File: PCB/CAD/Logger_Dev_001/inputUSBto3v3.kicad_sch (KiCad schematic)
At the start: 32 parts, among them J4 Connector, USB-TYPE-C-16P, Q1 BC847BS, U5 AMS1117, U6 CP2102-GMR

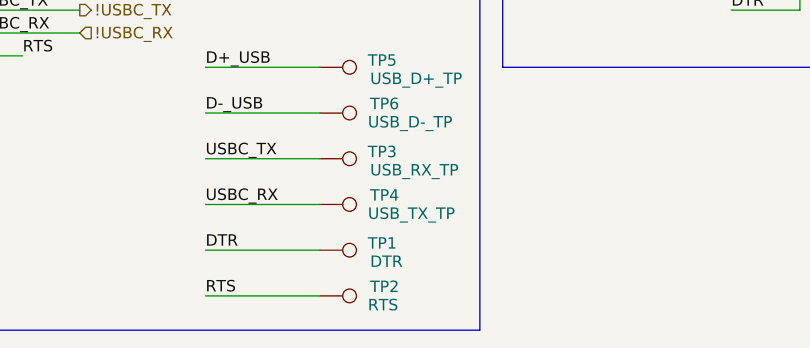
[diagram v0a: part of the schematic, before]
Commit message: Update some footprints
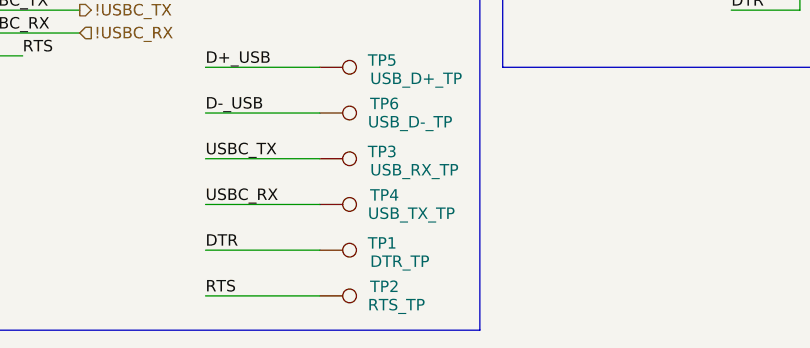
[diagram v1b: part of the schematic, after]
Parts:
- FL1: footprint DLM11SN900HY2L:FIL_DLM11SN900HY2L -> Common mode choke DLM11SN900HY2L:FIL_DLM11SN900HY2L
- TP1: value DTR -> DTR_TP
- TP2: value RTS -> RTS_TP
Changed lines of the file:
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@@
 			)
 		)
-		(property "Value" "DTR"
+		(property "Value" "DTR_TP"
 			(at 142.748 185.42 90)
 			(effects
@@
 			)
 		)
-		(property "Footprint" "DLM11SN900HY2L:FIL_DLM11SN900HY2L"
+		(property "Footprint" "Common mode choke DLM11SN900HY2L:FIL_DLM11SN900HY2L"
 			(at 119.38 49.53 0)
 			(effects
@@
 			)
 		)
-		(property "Value" "RTS"
+		(property "Value" "RTS_TP"
 			(at 142.494 190.246 90)
 			(effects

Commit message: Schematic Finished
Still need to check BOM
Starting to layout PCB
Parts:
- TP1, TP2, TP3, TP4, TP5, TP6: footprint (none) -> TestPoint:TestPoint_Pad_D2.5mm
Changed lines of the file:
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@@
 			)
 		)
-		(property "Footprint" ""
+		(property "Footprint" "TestPoint:TestPoint_Pad_D2.5mm"
 			(at 137.16 184.15 0)
 			(effects
@@
 			)
 		)
-		(property "Footprint" ""
+		(property "Footprint" "TestPoint:TestPoint_Pad_D2.5mm"
 			(at 137.16 168.91 0)
 			(effects
@@
 			)
 		)
-		(property "Footprint" ""
+		(property "Footprint" "TestPoint:TestPoint_Pad_D2.5mm"
 			(at 137.16 158.75 0)
 			(effects
@@
 			)
 		)
-		(property "Footprint" ""
+		(property "Footprint" "TestPoint:TestPoint_Pad_D2.5mm"
 			(at 137.16 179.07 0)
 			(effects
@@
 			)
 		)
-		(property "Footprint" ""
+		(property "Footprint" "TestPoint:TestPoint_Pad_D2.5mm"
 			(at 137.16 194.31 0)
 			(effects
@@
 			)
 		)
-		(property "Footprint" ""
+		(property "Footprint" "TestPoint:TestPoint_Pad_D2.5mm"
 			(at 137.16 173.99 0)
 			(effects

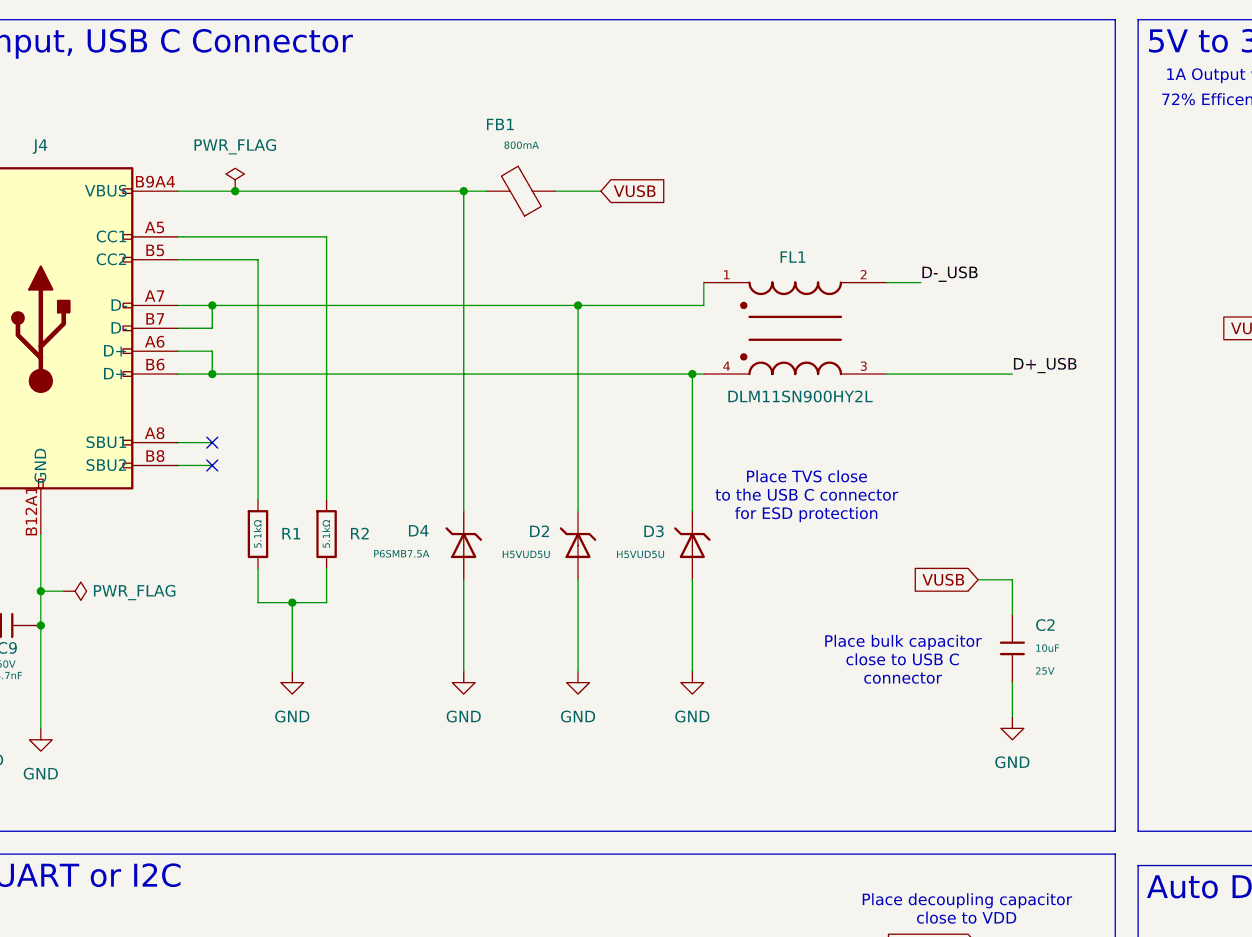
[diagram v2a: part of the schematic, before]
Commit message: PCB Layout Update
PCB Board Fixed
Most Components except Resistors placed
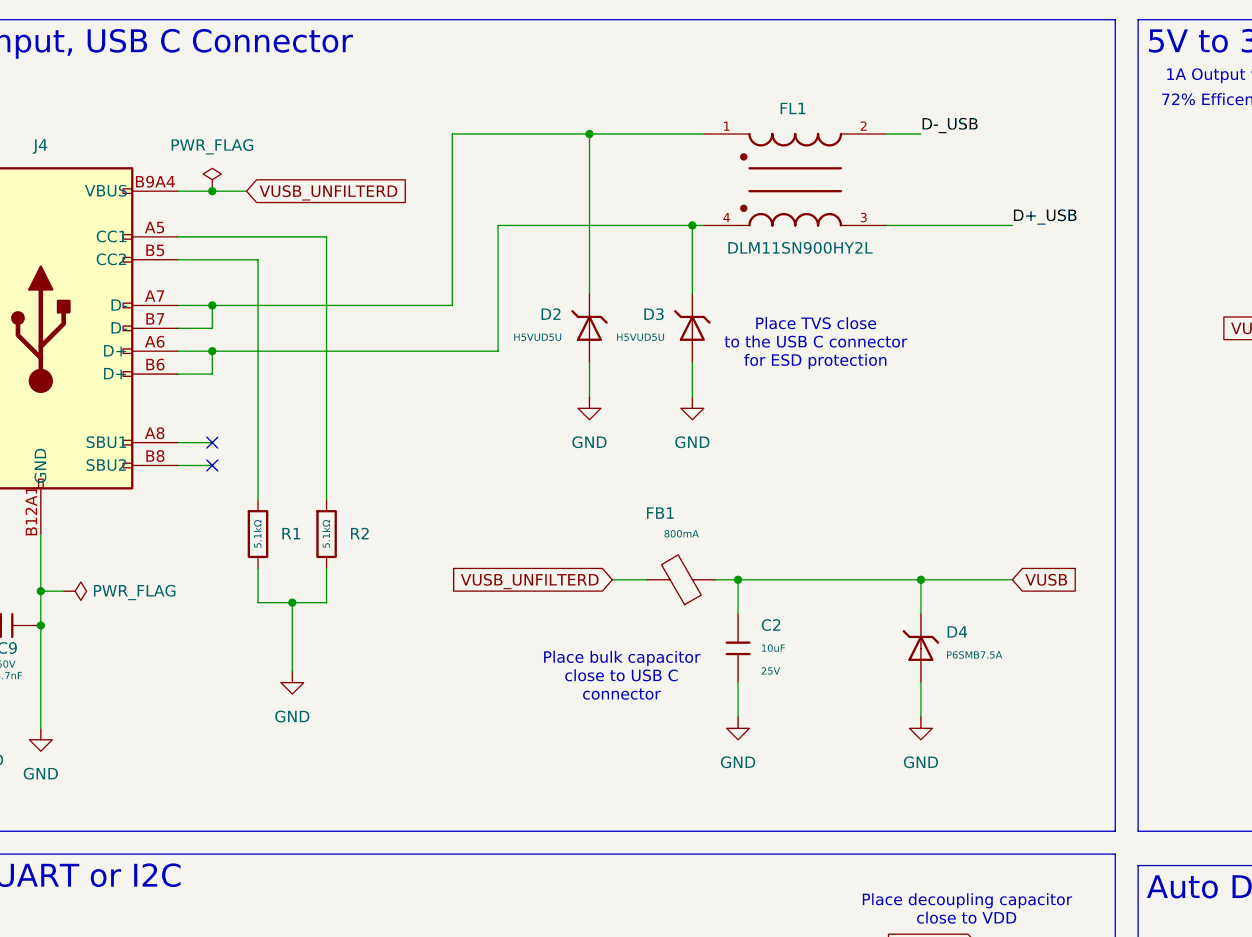
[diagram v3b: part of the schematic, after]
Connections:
- net VUSB: now also D4.1
- net VUSB_UNFILTERD: now reaches FB1.2, J4.A9B4 (VBUS), J4.B9A4 (VBUS)
- net VUSB_UNFILTERD: no longer D4.1
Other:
- moved on the sheet: C2, D2, D3, D4, FB1, FL1

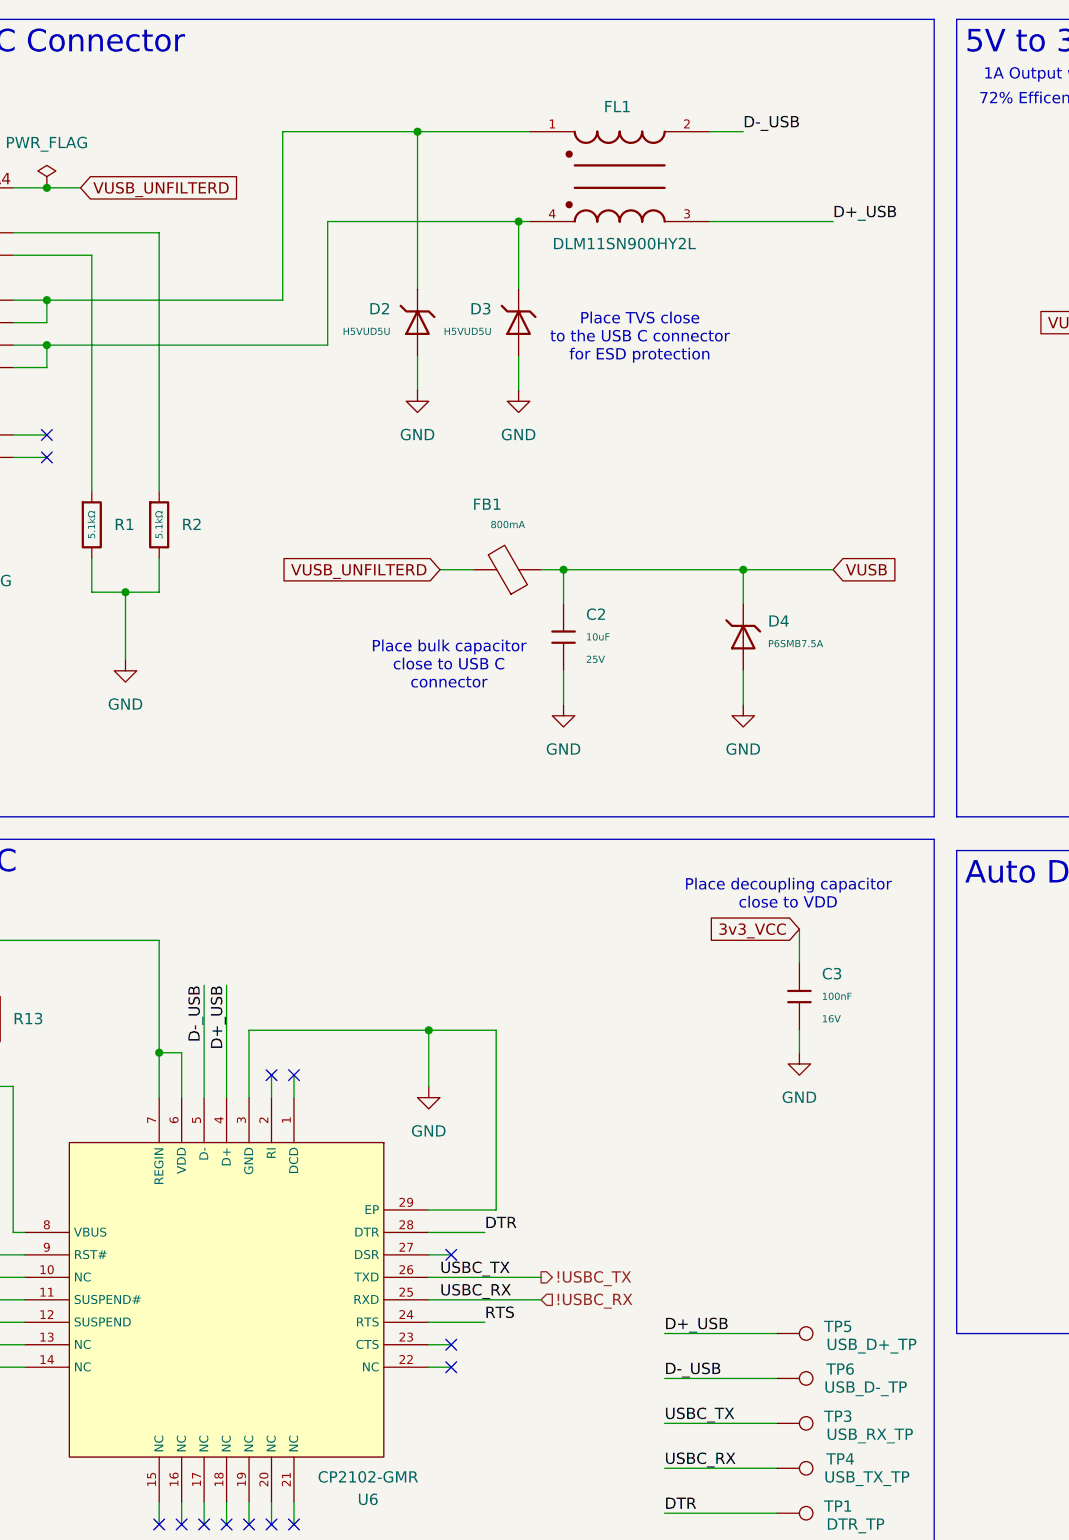
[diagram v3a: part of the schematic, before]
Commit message: PCB Board Initial Trace
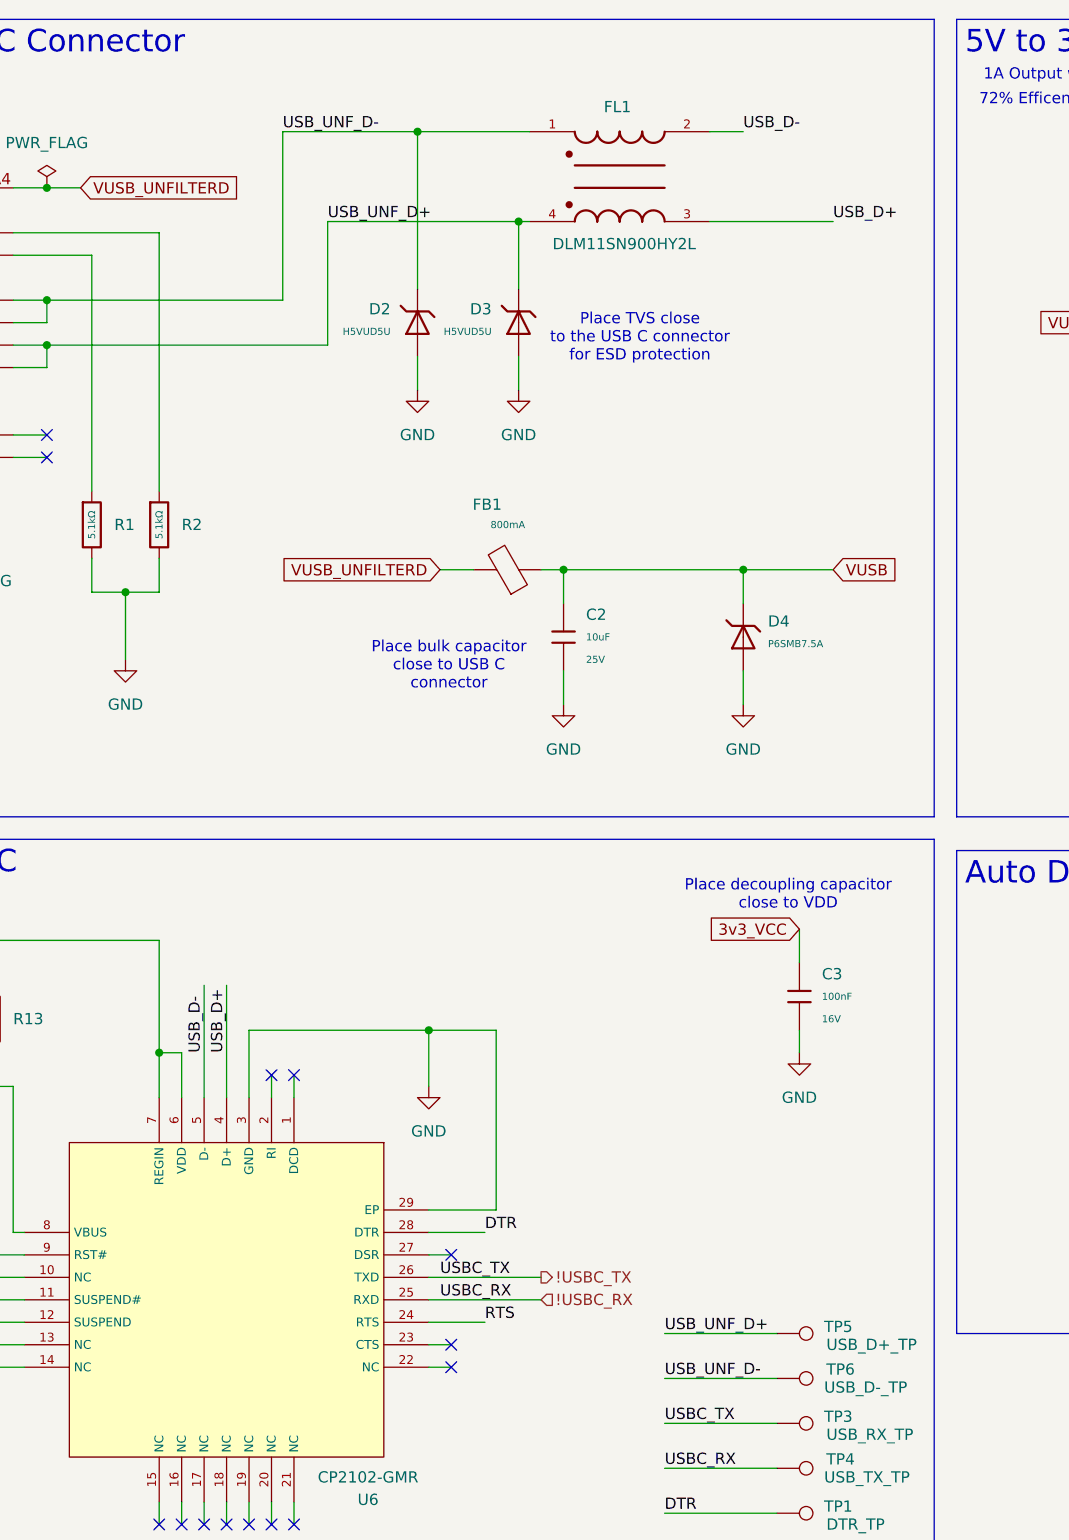
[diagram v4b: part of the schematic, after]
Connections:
- net USB_UNF_D+: now reaches D3.1, FL1.4, J4.A6 (D+), J4.B6 (D+)
- net USB_UNF_D+: now also TP5.1
- net USB_UNF_D-: now reaches D2.1, FL1.1, J4.A7 (D-), J4.B7 (D-)
- net USB_UNF_D-: now also TP6.1
- net D+_USB renamed USB_D+
- net USB_D+: no longer TP5.1
- net D-_USB renamed USB_D-
- net USB_D-: no longer TP6.1
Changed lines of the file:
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@@
 	(wire
 		(pts
-			(xy 67.31 68.58) (xy 67.31 39.37)
+			(xy 67.31 39.37) (xy 67.31 68.58)
 		)
 		(stroke
@@
 		)
 	)
-	(label "D+_USB"
+	(label "USB_UNF_D+"
+		(at 86.36 38.1 0)
+		(effects
+			(font
+				(size 1.27 1.27)
+			)
+			(justify left bottom)
+		)
+	)
+	(label "USB_UNF_D+"
 		(at 124.46 163.83 0)
 		(effects
@@
 		)
 	)
-	(label "D-_USB"
+	(label "USB_D-"
 		(at 133.35 27.94 0)
+		(effects
+			(font
+				(size 1.27 1.27)
+			)
+			(justify left bottom)
+		)
+	)
+	(label "USB_D+"
+		(at 74.93 132.08 90)
 		(effects
 			(font
@@
 		)
 	)
-	(label "D+_USB"
-		(at 74.93 124.46 270)
-		(effects
-			(font
-				(size 1.27 1.27)
-			)
-			(justify right bottom)
-		)
-	)
-	(label "D-_USB"
+	(label "USB_UNF_D-"
 		(at 124.46 168.91 0)
 		(effects
@@
 		)
 	)
+	(label "USB_UNF_D-"
+		(at 81.28 27.94 0)
+		(effects
+			(font
+				(size 1.27 1.27)
+			)
+			(justify left bottom)
+		)
+	)
 	(label "USBC_TX"
 		(at 124.46 173.99 0)
@@
 		)
 	)
-	(label "D-_USB"
-		(at 72.39 124.46 270)
-		(effects
-			(font
-				(size 1.27 1.27)
-			)
-			(justify right bottom)
-		)
-	)
-	(label "D+_USB"
+	(label "USB_D-"
+		(at 72.39 132.08 90)
+		(effects
+			(font
+				(size 1.27 1.27)
+			)
+			(justify left bottom)
+		)
+	)
+	(label "USB_D+"
 		(at 143.51 38.1 0)
 		(effects
@@
 		(polyline
 			(pts
+				(xy 57.15 59.69) (xy 57.15 72.39) (xy 74.93 72.39) (xy 74.93 62.23) (xy 69.85 59.69)
+			)
+			(stroke
+				(width 0)
+				(type dash)
+			)
+			(fill
+				(type none)
+			)
+		)
+	)
+	(rule_area
+		(polyline
+			(pts
 				(xy 231.14 38.1) (xy 231.14 59.69) (xy 278.13 59.69) (xy 278.13 44.45) (xy 271.78 38.1)
 			)
@@
 			(effects
 				(font
+					(size 1.27 1.27)
+					(italic yes)
+				)
+				(justify left)
+			)
+		)
+	)
+	(netclass_flag ""
+		(length 2.54)
+		(shape round)
+		(at 69.85 59.69 0)
+		(effects
+			(font
+				(size 1.27 1.27)
+			)
+			(justify left bottom)
+		)
+		(property "Netclass" "Signal"
+			(at 75.692 55.118 0)
+			(effects
+				(font
+					(size 1.27 1.27)
+				)
+				(justify right)
+			)
+		)
+		(property "Component Class" ""
+			(at 280.67 -48.26 0)
+			(effects
+				(font

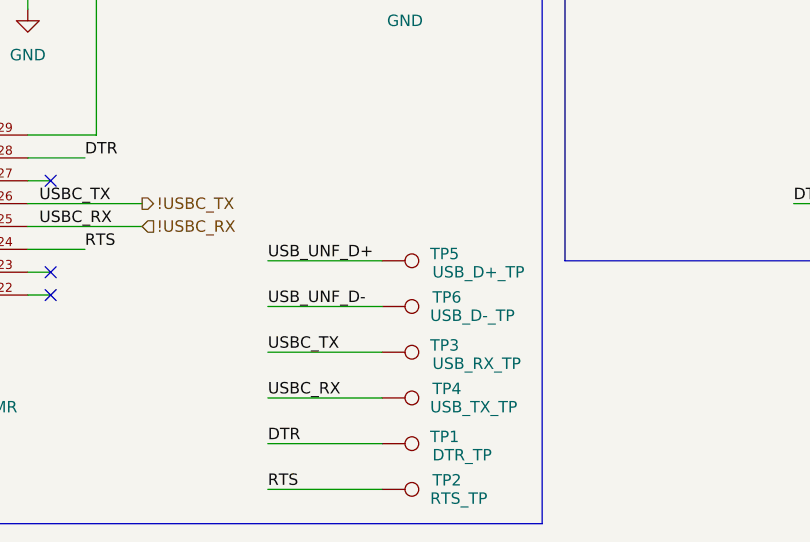
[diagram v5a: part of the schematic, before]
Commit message: BCB Board Update
Planes poured and general wiring completed. All vias updated. 3D models completed.

To check:
- footprints
- rules
-BOM cost
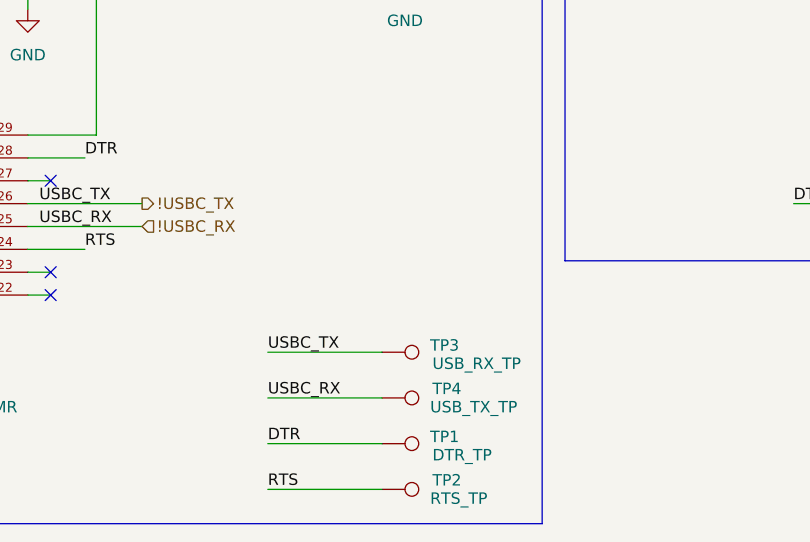
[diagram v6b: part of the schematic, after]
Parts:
- removed TP5: USB_D+_TP, TestPoint:TestPoint_Pad_D2.5mm, symbol Connector:TestPoint
- removed TP6: USB_D-_TP, TestPoint:TestPoint_Pad_D2.5mm, symbol Connector:TestPoint
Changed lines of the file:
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@@
 	(wire
 		(pts
-			(xy 124.46 168.91) (xy 137.16 168.91)
-		)
-		(stroke
-			(width 0)
-			(type default)
-		)
-	)
-	(wire
-		(pts
 			(xy 54.61 52.07) (xy 54.61 54.61)
 		)
@@
 	(wire
 		(pts
-			(xy 124.46 163.83) (xy 137.16 163.83)
-		)
-		(stroke
-			(width 0)
-			(type default)
-		)
-	)
-	(wire
-		(pts
 			(xy 72.39 182.88) (xy 72.39 185.42)
 		)
@@
 		)
 	)
-	(label "USB_UNF_D+"
-		(at 124.46 163.83 0)
-		(effects
-			(font
-				(size 1.27 1.27)
-			)
-			(justify left bottom)
-		)
-	)
 	(label "DTR"
 		(at 182.88 157.48 0)
@@
 		)
 	)
-	(label "USB_UNF_D-"
-		(at 124.46 168.91 0)
-		(effects
-			(font
-				(size 1.27 1.27)
-			)
-			(justify left bottom)
-		)
-	)
 	(label "USBC_RX"
 		(at 124.46 179.07 0)
@@
 	)
 	(symbol
-		(lib_id "Connector:TestPoint")
-		(at 137.16 163.83 270)
-		(mirror x)
-		(unit 1)
-		(exclude_from_sim no)
-		(in_bom yes)
-		(on_board yes)
-		(dnp no)
-		(property "Reference" "TP5"
-			(at 142.494 163.068 90)
-			(effects
-				(font
-					(size 1.27 1.27)
-				)
-				(justify left)
-			)
-		)
-		(property "Value" "USB_D+_TP"
-			(at 142.748 165.1 90)
-			(effects
-				(font
-					(size 1.27 1.27)
-				)
-				(justify left)
-			)
-		)
-		(property "Footprint" "TestPoint:TestPoint_Pad_D2.5mm"
-			(at 137.16 158.75 0)
-			(effects
-				(font
-					(size 1.27 1.27)
-				)
-				(hide yes)
-			)
-		)
-		(property "Datasheet" "~"
-			(at 137.16 158.75 0)
-			(effects
-				(font
-					(size 1.27 1.27)
-				)
-				(hide yes)
-			)
-		)
-		(property "Description" "test point"
-			(at 137.16 163.83 0)
-			(effects
-				(font
-					(size 1.27 1.27)
-				)
-				(hide yes)
-			)
-		)
-		(pin "1"
-		)
-		(instances
-			(project "Logger_Dev_001"
-				(path "/9546b831-c7ee-4f40-8993-5fd5a38d4078/588c330f-0a28-4ec5-8e7c-c377534893c3"
-					(reference "TP5")
-					(unit 1)
-				)
-			)
-		)
-	)
-	(symbol
 		(lib_id "power:GND")
 		(at 203.2 83.82 0)
@@
 					(unit 1)
 				)
-			)
-		)
-	)
-	(symbol
-		(lib_id "Connector:TestPoint")
-		(at 137.16 168.91 270)
-		(unit 1)
-		(exclude_from_sim no)
-		(in_bom yes)
-		(on_board yes)
-		(dnp no)
-		(property "Reference" "TP6"
-			(at 142.748 167.894 90)
-			(effects
-				(font
-					(size 1.27 1.27)
-				)
-				(justify left)
-			)
-		)
-		(property "Value" "USB_D-_TP"
-			(at 142.494 169.926 90)
-			(effects
-				(font
-					(size 1.27 1.27)
-				)
-				(justify left)
-			)
-		)
-		(property "Footprint" "TestPoint:TestPoint_Pad_D2.5mm"
-			(at 137.16 173.99 0)
-			(effects
-				(font
-					(size 1.27 1.27)
-				)
-				(hide yes)
-			)
-		)
-		(property "Datasheet" "~"
-			(at 137.16 173.99 0)
-			(effects
-				(font
-					(size 1.27 1.27)
-				)
-				(hide yes)
-			)
-		)
-		(property "Description" "test point"
-			(at 137.16 168.91 0)
-			(effects
-				(font
-					(size 1.27 1.27)
-				)
-				(hide yes)
-			)
-		)
-		(pin "1"
-		)
-		(instances
-			(project "Logger_Dev_001"
-				(path "/9546b831-c7ee-4f40-8993-5fd5a38d4078/588c330f-0a28-4ec5-8e7c-c377534893c3"
-					(reference "TP6")
-					(unit 1)
-				)
